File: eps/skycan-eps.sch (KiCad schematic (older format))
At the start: 41 parts, among them J1 DF9-25P-1V-PLUG, J2 DF9-25P-1V-SOCKET, J3 DF9-25P-1V-PLUG, J4 DF9-25P-1V-SOCKET, U1 TPS63060, U2 BQ27210, U3 MICRO-B_USB, U4 MCP73831, U5 SWITCH-DPDT

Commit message: EPS board now uses only skycan lib.
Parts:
- removed J1, J3: DF9-25P-1V-PLUG, symbol DF9-25P-1V-PLUG
- removed J2, J4: DF9-25P-1V-SOCKET, symbol DF9-25P-1V-SOCKET
- added J1, J3: DF9_25P_1V_PLUG, symbol DF9_25P_1V_PLUG
- added J2, J4: DF9_25P_1V_SOCKET, symbol DF9_25P_1V_SOCKET
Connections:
- wire segments 135 -> 139
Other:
- moved on the sheet: C14, D1, R10, R9

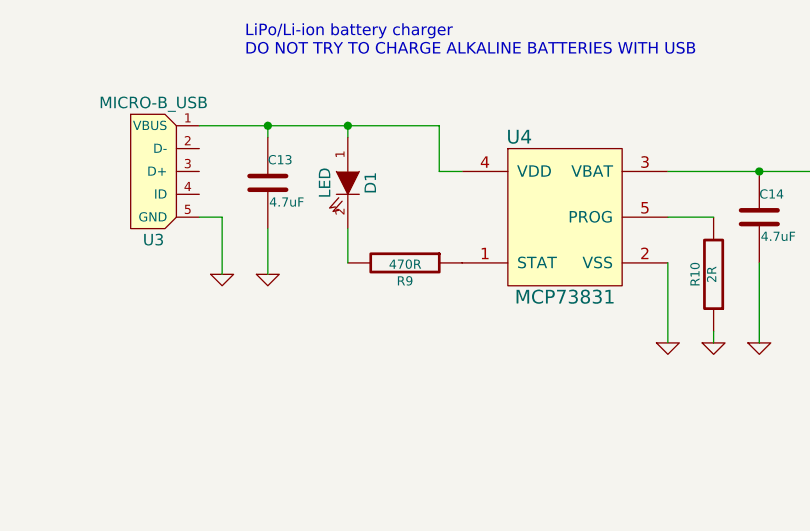
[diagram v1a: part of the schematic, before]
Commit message: Added Farnell codes to EPS schematic
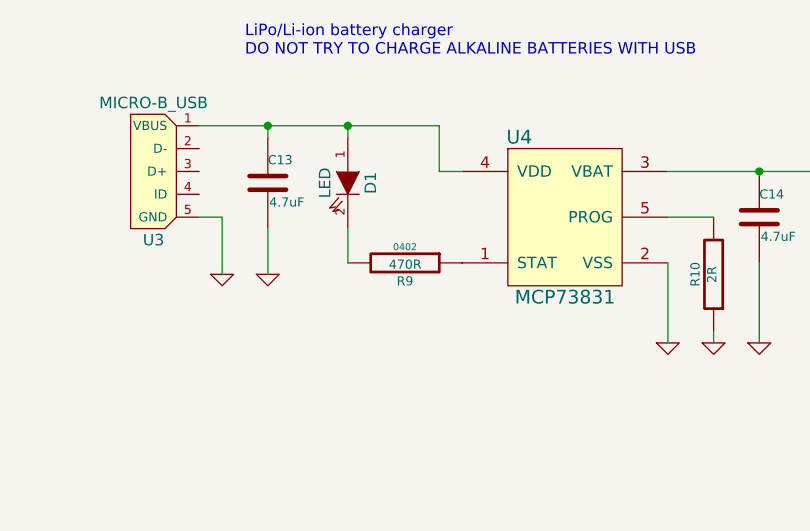
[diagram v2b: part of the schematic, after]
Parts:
- BT1: footprint (none) -> AA holder
- BT2: footprint (none) -> LiPo; Farnell 1339843 -> (none)
- C1, C13, C14, C2, C5, C6, C7: footprint (none) -> 0805
- C10, C11, C12, C3, C4, C8, C9, R1, R10, R2, R3, R4, R5, R6, R7, R9: footprint (none) -> 0402
- D1, R8: footprint (none) -> 0603
- J1, J3: Farnell (none) -> 1798379
- J2, J4: Farnell (none) -> 1798380
- L1: footprint (none) -> 4x4 mm
- U1: footprint (none) -> PWSON-N10; Farnell (none) -> 2082430
- U2: footprint (none) -> PVSON-N10; Farnell (none) -> 1754768
- U3: Farnell (none) -> 2293753
- U4: footprint (none) -> SOT-23-5; Farnell (none) -> 1332158
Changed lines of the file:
@@
 Sheet 1 1
 Title "EPS"
-Date "11 sept  2013"
+Date "15 sept  2013"
 Rev "1.0"
 Comp "Skycan"
@@
 F 0 "U1" H 11850 7900 60  0000 C CNN
 F 1 "TPS63060" H 12200 6950 60  0000 C CNN
-F 2 "" H 12200 7550 60  0000 C CNN
+F 2 "PWSON-N10" H 12200 7550 60  0001 C CNN
 F 3 "" H 12200 7550 60  0000 C CNN
+F 4 "2082430" H 12200 7550 60  0001 C CNN "Farnell"
 	1    12200 7550
 	1    0    0    -1
@@
 F 0 "L1" H 12200 7050 50  0000 C CNN
 F 1 "1uH" H 12200 6900 50  0000 C CNN
-F 2 "" H 12200 6950 60  0000 C CNN
+F 2 "4x4 mm" H 12200 6950 60  0001 C CNN
 F 3 "" H 12200 6950 60  0000 C CNN
 F 4 "2289214" H 12200 6950 60  0001 C CNN "Farnell"
@@
 F 0 "C3" H 11450 7950 40  0000 L CNN
 F 1 "100nF" H 11456 7765 40  0000 L CNN
-F 2 "" H 11488 7700 30  0000 C CNN
+F 2 "0402" H 11488 7700 30  0001 C CNN
 F 3 "" H 11450 7850 60  0000 C CNN
 	1    11450 7850
@@
 F 0 "C2" H 11200 7950 40  0000 L CNN
 F 1 "10uF" H 11206 7765 40  0000 L CNN
-F 2 "" H 11238 7700 30  0000 C CNN
+F 2 "0805" H 11238 7700 30  0001 C CNN
 F 3 "" H 11200 7850 60  0000 C CNN
 	1    11200 7850
@@
 F 0 "C1" H 10950 7950 40  0000 L CNN
 F 1 "10uF" H 10956 7765 40  0000 L CNN
-F 2 "" H 10988 7700 30  0000 C CNN
+F 2 "0805" H 10988 7700 30  0001 C CNN
 F 3 "" H 10950 7850 60  0000 C CNN
 	1    10950 7850
@@
 F 0 "R1" V 13230 7700 40  0000 C CNN
 F 1 "1M" V 13157 7701 40  0000 C CNN
-F 2 "" V 13080 7700 30  0000 C CNN
+F 2 "0402" V 13080 7700 30  0001 C CNN
 F 3 "" H 13150 7700 30  0000 C CNN
 	1    13150 7700
@@
 F 0 "R2" V 13230 8200 40  0000 C CNN
 F 1 "168k" V 13157 8201 40  0000 C CNN
-F 2 "" V 13080 8200 30  0000 C CNN
+F 2 "0402" V 13080 8200 30  0001 C CNN
 F 3 "" H 13150 8200 30  0000 C CNN
 	1    13150 8200
@@
 F 0 "C4" H 13350 8250 40  0000 L CNN
 F 1 "10pF" H 13356 8065 40  0000 L CNN
-F 2 "" H 13388 8000 30  0000 C CNN
+F 2 "0402" H 13388 8000 30  0001 C CNN
 F 3 "" H 13350 8150 60  0000 C CNN
 	1    13350 8150
@@
 F 0 "R3" V 13630 7700 40  0000 C CNN
 F 1 "100k" V 13557 7701 40  0000 C CNN
-F 2 "" V 13480 7700 30  0000 C CNN
+F 2 "0402" V 13480 7700 30  0001 C CNN
 F 3 "" H 13550 7700 30  0000 C CNN
 	1    13550 7700
@@
 F 0 "C5" H 13850 7900 40  0000 L CNN
 F 1 "22uF" H 13856 7715 40  0000 L CNN
-F 2 "" H 13888 7650 30  0000 C CNN
+F 2 "0805" H 13888 7650 30  0001 C CNN
 F 3 "" H 13850 7800 60  0000 C CNN
 	1    13850 7800
@@
 F 0 "C6" H 14100 7900 40  0000 L CNN
 F 1 "22uF" H 14106 7715 40  0000 L CNN
-F 2 "" H 14138 7650 30  0000 C CNN
+F 2 "0805" H 14138 7650 30  0001 C CNN
 F 3 "" H 14100 7800 60  0000 C CNN
 	1    14100 7800
@@
 F 0 "C7" H 14350 7900 40  0000 L CNN
 F 1 "22uF" H 14356 7715 40  0000 L CNN
-F 2 "" H 14388 7650 30  0000 C CNN
+F 2 "0805" H 14388 7650 30  0001 C CNN
 F 3 "" H 14350 7800 60  0000 C CNN
 	1    14350 7800
@@
 F 0 "BT1" H 13650 4150 50  0000 C CNN
 F 1 "3x1.5V AAA" H 13650 3760 50  0000 C CNN
-F 2 "" H 13650 3950 60  0000 C CNN
+F 2 "AA holder" H 13650 3950 60  0001 C CNN
 F 3 "" H 13650 3950 60  0000 C CNN
 F 4 "1339843" H 13650 3950 60  0001 C CNN "Farnell"
@@
 F 0 "R6" V 13480 4300 40  0000 C CNN
 F 1 "1M" V 13407 4301 40  0000 C CNN
-F 2 "" V 13330 4300 30  0000 C CNN
+F 2 "0402" V 13330 4300 30  0001 C CNN
 F 3 "" H 13400 4300 30  0000 C CNN
 	1    13400 4300
@@
 F 0 "C12" H 13050 4600 40  0000 L CNN
 F 1 "100nF" H 13056 4415 40  0000 L CNN
-F 2 "" H 13088 4350 30  0000 C CNN
+F 2 "0402" H 13088 4350 30  0001 C CNN
 F 3 "" H 13050 4500 60  0000 C CNN
 	1    13050 4500
@@
 F 0 "R7" V 13480 4900 40  0000 C CNN
 F 1 "1M" V 13407 4901 40  0000 C CNN
-F 2 "" V 13330 4900 30  0000 C CNN
+F 2 "0402" V 13330 4900 30  0001 C CNN
 F 3 "" H 13400 4900 30  0000 C CNN
 	1    13400 4900
@@
 F 0 "C11" H 12900 5200 40  0000 L CNN
 F 1 "100nF" H 12906 5015 40  0000 L CNN
-F 2 "" H 12938 4950 30  0000 C CNN
+F 2 "0402" H 12938 4950 30  0001 C CNN
 F 3 "" H 12900 5100 60  0000 C CNN
 	1    12900 5100
@@
 F 0 "C10" H 12700 4900 40  0000 L CNN
 F 1 "100nF" H 12706 4715 40  0000 L CNN
-F 2 "" H 12738 4650 30  0000 C CNN
+F 2 "0402" H 12738 4650 30  0001 C CNN
 F 3 "" H 12700 4800 60  0000 C CNN
 	1    12700 4800
@@
 F 0 "R8" V 13730 4600 40  0000 C CNN
 F 1 "0.02R" V 13657 4601 40  0000 C CNN
-F 2 "" V 13580 4600 30  0000 C CNN
+F 2 "0603" V 13580 4600 30  0001 C CNN
 F 3 "" H 13650 4600 30  0000 C CNN
 	1    13650 4600
@@
 F 0 "R5" V 12780 3800 40  0000 C CNN
 F 1 "10k" V 12707 3801 40  0000 C CNN
-F 2 "" V 12630 3800 30  0000 C CNN
+F 2 "0402" V 12630 3800 30  0001 C CNN
 F 3 "" H 12700 3800 30  0000 C CNN
 	1    12700 3800
@@
 F 0 "C8" H 11150 5000 40  0000 L CNN
 F 1 "100nF" H 11156 4815 40  0000 L CNN
-F 2 "" H 11188 4750 30  0000 C CNN
+F 2 "0402" H 11188 4750 30  0001 C CNN
 F 3 "" H 11150 4900 60  0000 C CNN
 	1    11150 4900
@@
 F 0 "R4" V 11230 3800 40  0000 C CNN
 F 1 "1k" V 11157 3801 40  0000 C CNN
-F 2 "" V 11080 3800 30  0000 C CNN
+F 2 "0402" V 11080 3800 30  0001 C CNN
 F 3 "" H 11150 3800 30  0000 C CNN
 	1    11150 3800
@@
 F 0 "C9" H 11400 5000 40  0000 L CNN
 F 1 "100nF" H 11406 4815 40  0000 L CNN
-F 2 "" H 11438 4750 30  0000 C CNN
+F 2 "0402" H 11438 4750 30  0001 C CNN
 F 3 "" H 11400 4900 60  0000 C CNN
 	1    11400 4900
@@
 F 0 "U2" H 11950 4650 60  0000 C CNN
 F 1 "BQ27210" H 11850 3950 60  0000 C CNN
-F 2 "" H 12150 4300 60  0000 C CNN
+F 2 "PVSON-N10" H 12150 4300 60  0001 C CNN
 F 3 "" H 12150 4300 60  0000 C CNN
+F 4 "1754768" H 12150 4300 60  0001 C CNN "Farnell"
 	1    12150 4300
 	1    0    0    -1
@@
 F 0 "C14" H 10150 3850 40  0000 L CNN
 F 1 "4.7uF" H 10156 3665 40  0000 L CNN
-F 2 "" H 10188 3600 30  0000 C CNN
+F 2 "0805" H 10188 3600 30  0001 C CNN
 F 3 "" H 10150 3750 60  0000 C CNN
 	1    10150 3750
@@
 F 0 "R10" V 10030 4000 40  0000 C CNN
 F 1 "2R" V 9957 4001 40  0000 C CNN
-F 2 "" V 9880 4000 30  0000 C CNN
+F 2 "0402" V 9880 4000 30  0001 C CNN
 F 3 "" H 9950 4000 30  0000 C CNN
 	1    9950 4000
@@
 F 0 "D1" H 8350 3700 50  0000 C CNN
 F 1 "LED" H 8350 3500 50  0000 C CNN
-F 2 "" H 8350 3600 60  0000 C CNN
+F 2 "0603" H 8350 3600 60  0001 C CNN
 F 3 "" H 8350 3600 60  0000 C CNN
 	1    8350 3600
@@
 F 0 "R9" V 8680 3950 40  0000 C CNN
 F 1 "470R" V 8607 3951 40  0000 C CNN
-F 2 "" V 8530 3950 30  0000 C CNN
+F 2 "0402" V 8530 3950 30  0000 C CNN
 F 3 "" H 8600 3950 30  0000 C CNN
 	1    8600 3950
@@
 F 0 "C13" H 8000 3700 40  0000 L CNN
 F 1 "4.7uF" H 8006 3515 40  0000 L CNN
-F 2 "" H 8038 3450 30  0000 C CNN
+F 2 "0805" H 8038 3450 30  0001 C CNN
 F 3 "" H 8000 3600 60  0000 C CNN
 	1    8000 3600
@@
 F 0 "BT2" H 14200 4150 50  0000 C CNN
 F 1 "LiPo" H 14200 3760 50  0000 C CNN
-F 2 "" H 14200 3950 60  0000 C CNN
+F 2 "LiPo" H 14200 3950 60  0001 C CNN
 F 3 "" H 14200 3950 60  0000 C CNN
-F 4 "1339843" H 14200 3950 60  0001 C CNN "Farnell"
 	1    14200 3950
 	0    1    1    0
@@
 F 2 "" H 2850 7500 60  0000 C CNN
 F 3 "http://www.hirose.co.jp/cataloge_hp/e54000041.pdf" H 2900 7800 60  0001 C CNN
+F 4 "1798380" H 2950 6700 60  0001 C CNN "Farnell"
 	1    2950 6700
 	1    0    0    -1
@@
 F 2 "" H 4700 7500 60  0000 C CNN
 F 3 "http://www.hirose.co.jp/cataloge_hp/e54000041.pdf" H 4750 7800 60  0001 C CNN
+F 4 "1798380" H 4800 6700 60  0001 C CNN "Farnell"
 	1    4800 6700
 	1    0    0    -1
@@
 F 2 "" H 2850 4900 60  0000 C CNN
 F 3 "http://www.hirose.co.jp/cataloge_hp/e54000041.pdf" H 2900 5200 60  0001 C CNN
+F 4 "1798379" H 2950 4100 60  0001 C CNN "Farnell"
 	1    2950 4100
 	1    0    0    -1
@@
 F 2 "" H 4700 4900 60  0000 C CNN
 F 3 "http://www.hirose.co.jp/cataloge_hp/e54000041.pdf" H 4750 5200 60  0001 C CNN
+F 4 "1798379" H 4800 4100 60  0001 C CNN "Farnell"
 	1    4800 4100
 	1    0    0    -1
@@
 F 2 "" H 7500 3550 60  0000 C CNN
 F 3 "" H 7500 3550 60  0000 C CNN
+F 4 "2293753" H 7500 3550 60  0001 C CNN "Farnell"
 	1    7500 3550
 	1    0    0    -1
@@
 F 0 "U4" H 9100 4100 60  0000 C CNN
 F 1 "MCP73831" H 9300 3400 60  0000 C CNN
-F 2 "" H 9300 3750 60  0000 C CNN
+F 2 "SOT-23-5" H 9300 3750 60  0001 C CNN
 F 3 "" H 9300 3750 60  0000 C CNN
+F 4 "1332158" H 9300 3750 60  0001 C CNN "Farnell"
 	1    9300 3750
 	1    0    0    -1

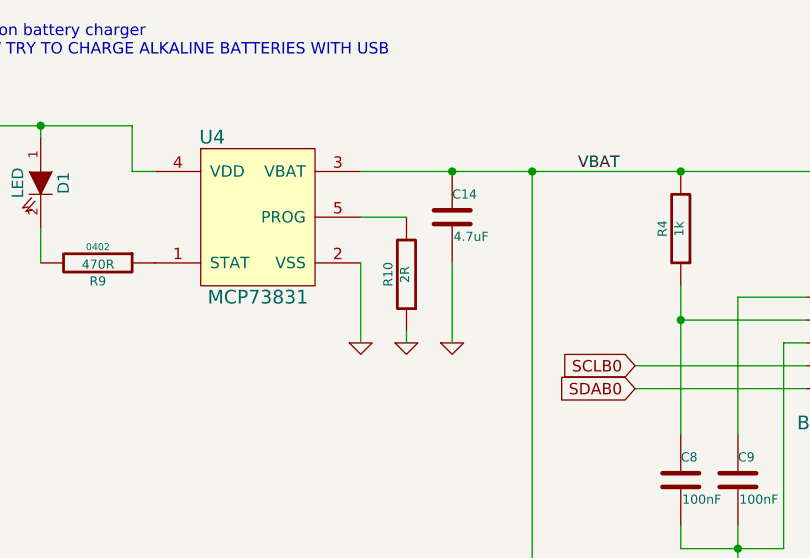
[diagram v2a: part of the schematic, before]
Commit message: Fixed EPS charger prog resistor value
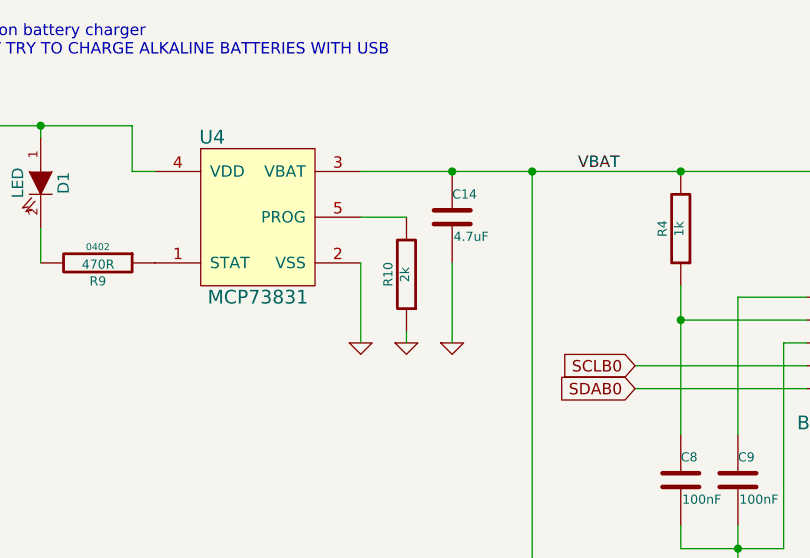
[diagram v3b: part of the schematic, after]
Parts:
- R10: value 2R -> 2k
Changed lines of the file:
@@
 P 9950 4000
 F 0 "R10" V 10030 4000 40  0000 C CNN
-F 1 "2R" V 9957 4001 40  0000 C CNN
+F 1 "2k" V 9957 4001 40  0000 C CNN
 F 2 "0402" V 9880 4000 30  0001 C CNN
 F 3 "" H 9950 4000 30  0000 C CNN

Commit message: Improved EPS main Vreg divider value
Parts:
- R2: value 168k -> 180k
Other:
- note added: "R1 = R2 * (3.3V/0.5V - 1)\nFrom DS page 21"
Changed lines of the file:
@@
 P 13150 8200
 F 0 "R2" V 13230 8200 40  0000 C CNN
-F 1 "168k" V 13157 8201 40  0000 C CNN
+F 1 "180k" V 13157 8201 40  0000 C CNN
 F 2 "0402" V 13080 8200 30  0001 C CNN
 F 3 "" H 13150 8200 30  0000 C CNN
@@
 	8350 3400 8350 3350
 Connection ~ 8350 3350
+Text Notes 12400 8850 0    50   ~ 0
+R1 = R2 * (3.3V/0.5V - 1)\nFrom DS page 21
 $EndSCHEMATC

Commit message: Added EPS power measurement resistor Farnell code
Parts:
- R8: Farnell (none) -> 1798577
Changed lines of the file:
@@
 F 2 "0603" V 13580 4600 30  0001 C CNN
 F 3 "" H 13650 4600 30  0000 C CNN
+F 4 "1798577" V 13650 4600 60  0001 C CNN "Farnell"
 	1    13650 4600
 	-1   0    0    1

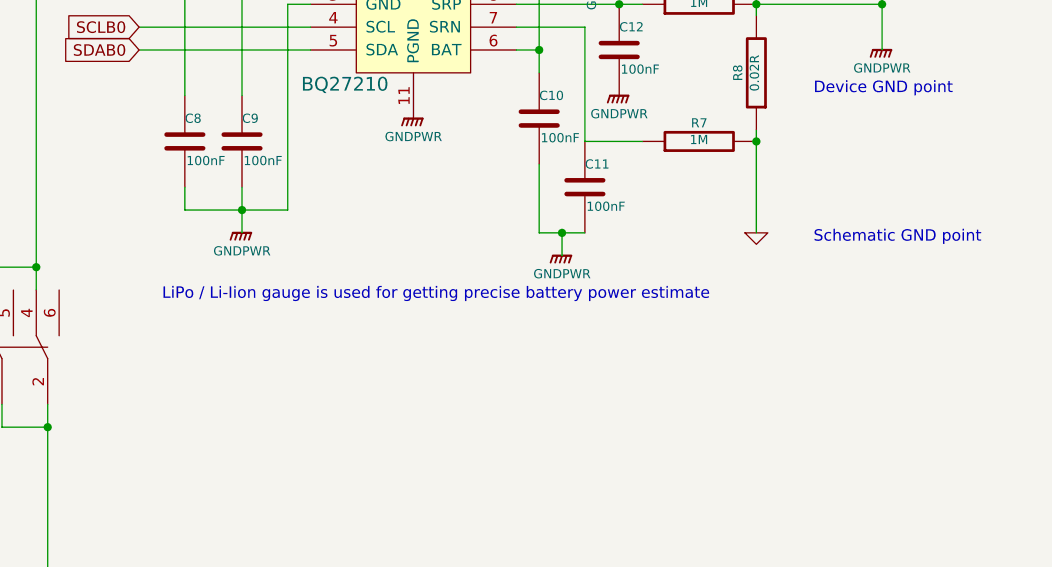
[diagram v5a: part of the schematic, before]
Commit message: Added I2C address info to EPS schem
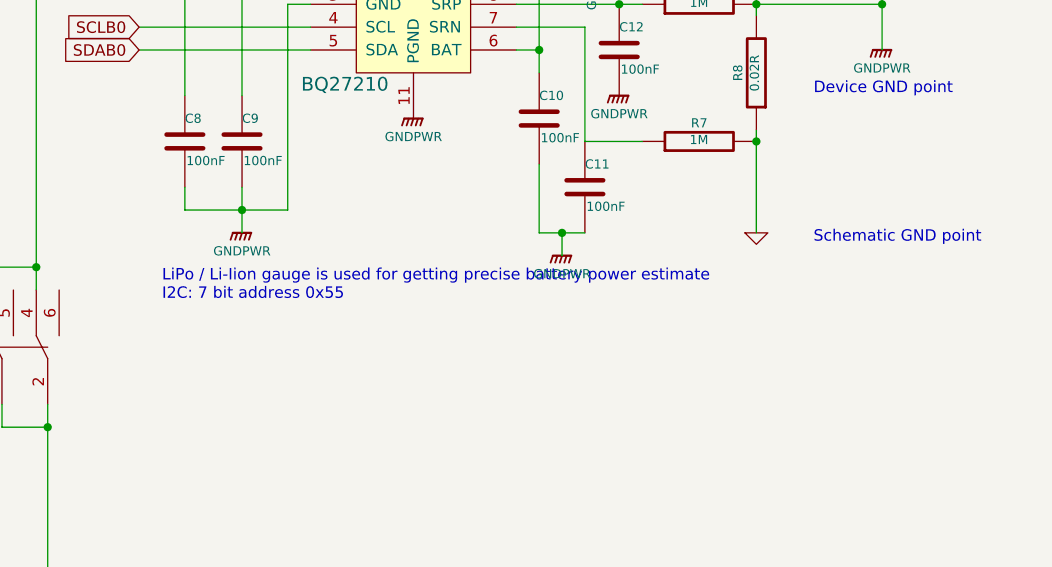
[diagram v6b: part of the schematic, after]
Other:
- note added: "LiPo / Li-Iion gauge is used for getting precise battery power estimate\nI2C: 7 bit address 0x55"
- note removed: "LiPo / Li-Iion gauge is used for getting precise battery power estimate"
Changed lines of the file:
@@
 SCLB0
 Text Notes 11050 5600 0    50   ~ 0
-LiPo / Li-Iion gauge is used for getting precise battery power estimate
+LiPo / Li-Iion gauge is used for getting precise battery power estimate\nI2C: 7 bit address 0x55
 Text Notes 13750 8850 0    50   ~ 0
 Not used
